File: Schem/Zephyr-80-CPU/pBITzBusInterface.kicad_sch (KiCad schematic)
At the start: 1 part, among them J1 pBITzBus

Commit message: synching
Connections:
- net ~{BUSREQ}: now reaches J1.A11 (CTRL_10)
- net ~{BUSACK}: now reaches J1.A12 (CTRL_11)
- net ~{CS_CART}: now reaches J1.A20 (CTRL_19)
- net A12: now reaches J1.A32 (A12)
- net A13: now reaches J1.A33 (A13)
- net A14: now reaches J1.A34 (A14)
- net A15: now reaches J1.A36 (A15)
- net PROG: now reaches J1.A8 (PROG)
- net ~{WR}: now reaches J1.B13 (CTRL_2)
- net ~{MREQ}: now reaches J1.B14 (CTRL_3)
- net ~{HALT}: now reaches J1.B18 (CTRL_7)
- net A2: now reaches J1.B34 (A2)
- net A3: now reaches J1.B36 (A3)
- net A4: now reaches J1.B37 (A4)
- net A5: now reaches J1.B38 (A5)
- net A6: now reaches J1.B40 (A6)
- net A7: now reaches J1.B41 (A7)
- net A8: now reaches J1.B42 (A8)
- net A9: now reaches J1.B44 (A9)
- net A10: now reaches J1.B45 (A10)
- net A11: now reaches J1.B46 (A11)
- net CART: now reaches J1.B8 (CART)
- net CTC_T01: no longer names the net of J1.A5 (CLK2)
- net CTC_T02: no longer names the net of J1.A6 (CLK3)
- net IEI: no longer names the net of J1.A18 (CTRL_17)
- net IEO: no longer names the net of J1.A19 (CTRL_18)
- net SD_PRESENT: no longer names the net of J1.B7 (SPI_CD)
- net SPI_CLK: no longer names the net of J1.A7 (SPI_CLK)
- net SPI_CS0: no longer names the net of J1.A49 (SPI_CS0)
- net SPI_CS1: no longer names the net of J1.B49 (SPI_CS1)
- net SPI_MISO: no longer names the net of J1.A48 (MISO)
- net SPI_MOSI: no longer names the net of J1.B48 (MOSI)
- net USB_INT: no longer names the net of J1.A47 (~{SPI_INT})
- net ~{POWER_OFF_RQ}: no longer names the net of J1.A3 (~{PWR_OFF_RQ})
- net ~{POWER_OFF}: no longer names the net of J1.B3 (~{PWR_OFF})
- no-connect marks 48 -> 39

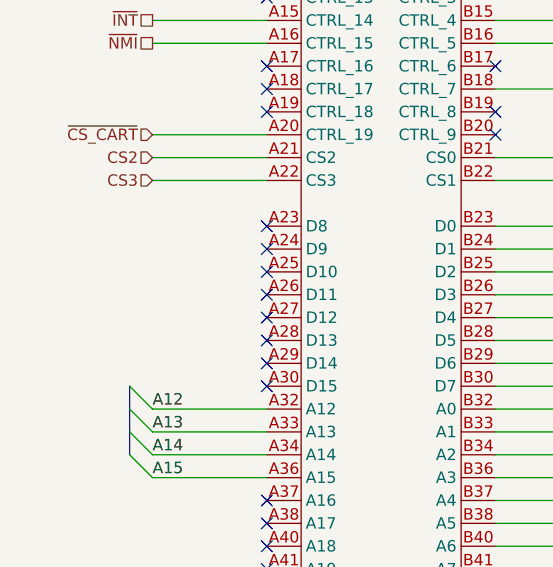
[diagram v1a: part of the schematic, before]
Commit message: Routed the CPU board. Removed the rotary switches decoder
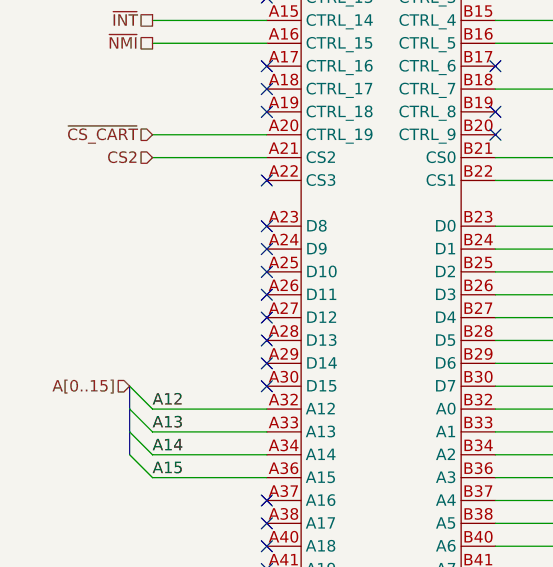
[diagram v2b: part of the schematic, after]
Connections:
- net CS3: no longer names the net of J1.A22 (CS3)
- no-connect marks 39 -> 40
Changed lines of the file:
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@@
 		(at 107.95 130.81)
+	)
+	(no_connect
+		(at 107.95 166.37)
 	)
 	(bus_entry
@@
 		(pts
 			(xy 133.35 212.09) (xy 146.05 212.09)
-		)
-		(stroke
-			(width 0)
-			(type default)
-		)
-	)
-	(wire
-		(pts
-			(xy 95.25 166.37) (xy 107.95 166.37)
 		)
 		(stroke
@@
 		)
 	)
-	(hierarchical_label "CS3"
-		(shape input)
-		(at 95.25 166.37 180)
-		(effects
-			(font
-				(size 1.27 1.27)
-			)
-			(justify right)
-		)
-	)
 	(hierarchical_label "CS2"
 		(shape input)
@@
 		)
 	)
+	(hierarchical_label "A[0..15]"
+		(shape input)
+		(at 92.71 189.23 180)
+		(effects
+			(font
+				(size 1.27 1.27)
+			)
+			(justify right)
+		)
+	)

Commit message: Added all the manufacturer part numbers to the KiCad schematics and PCB files. This will make it easier to order the parts for the project and ensure that the correct components are used. I also removed some of the old schematics that were no longer needed, such as the BaudClock, ConsolePort, DeviceSelectDecode, GPIOUserSerial, IO Controller, UserPorts, Video, and Z80HomeBrew schematics. These changes will help to streamline the design and make it easier to understand.
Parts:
- J1: now left out of the parts list
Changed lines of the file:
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@@
 		(unit 2)
 		(exclude_from_sim no)
-		(in_bom yes)
+		(in_bom no)
 		(on_board yes)
 		(dnp no)
@@
 		(unit 3)
 		(exclude_from_sim no)
-		(in_bom yes)
+		(in_bom no)
 		(on_board yes)
 		(dnp no)
@@
 		(unit 1)
 		(exclude_from_sim no)
-		(in_bom yes)
+		(in_bom no)
 		(on_board yes)
 		(dnp no)
